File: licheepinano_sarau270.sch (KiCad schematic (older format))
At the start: 0 parts

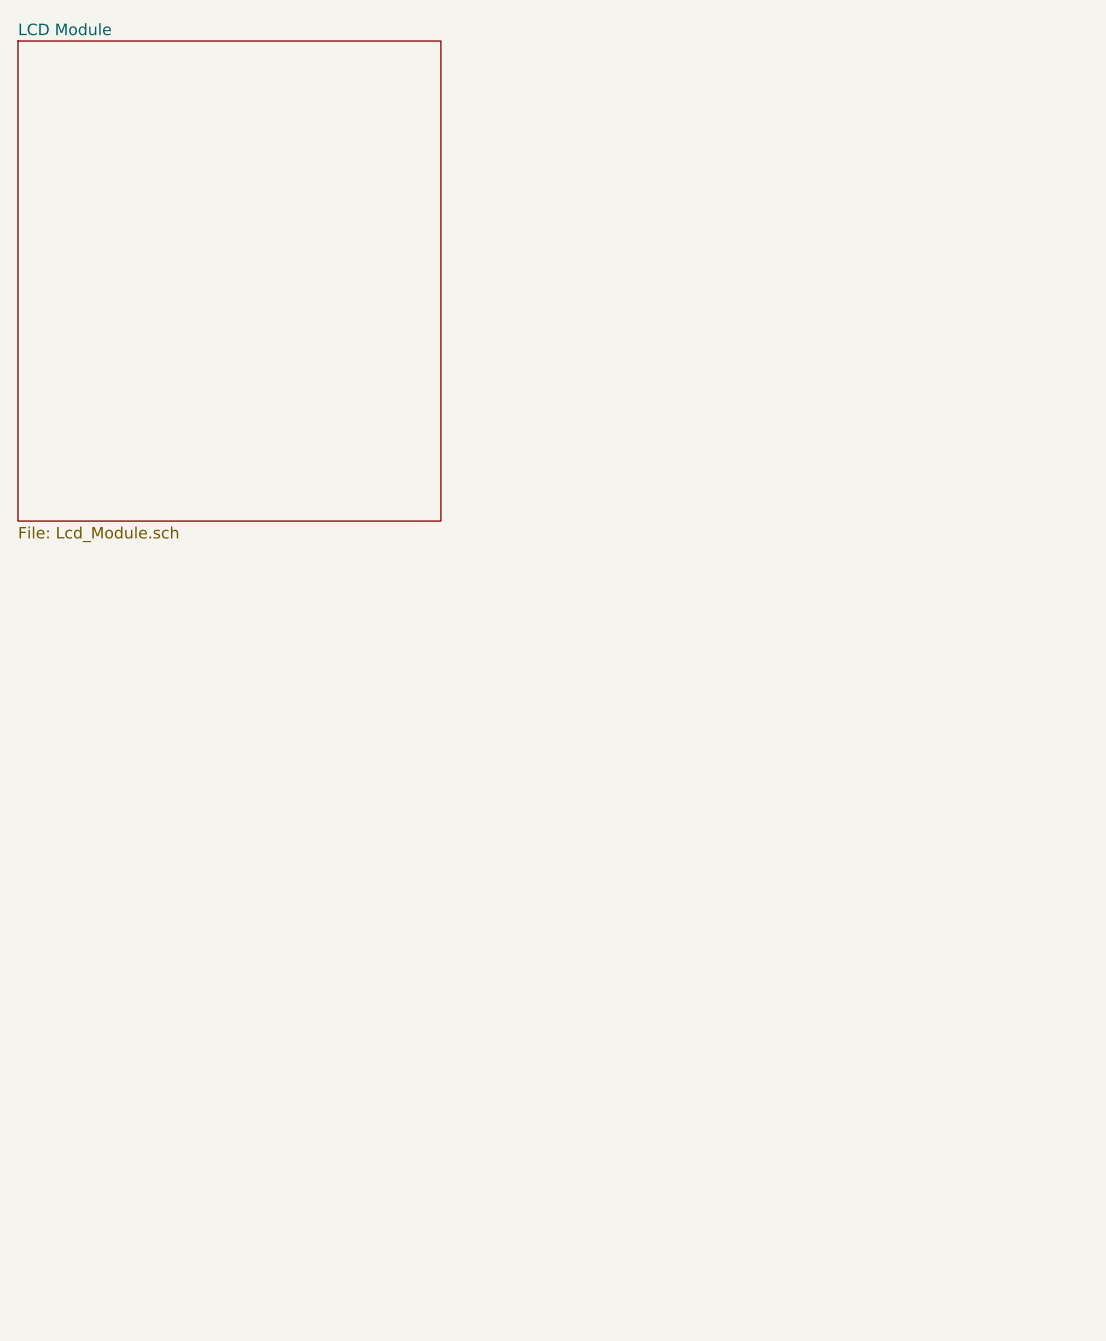
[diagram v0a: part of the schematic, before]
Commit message: Added Hub USB, Modem 3G and GPS
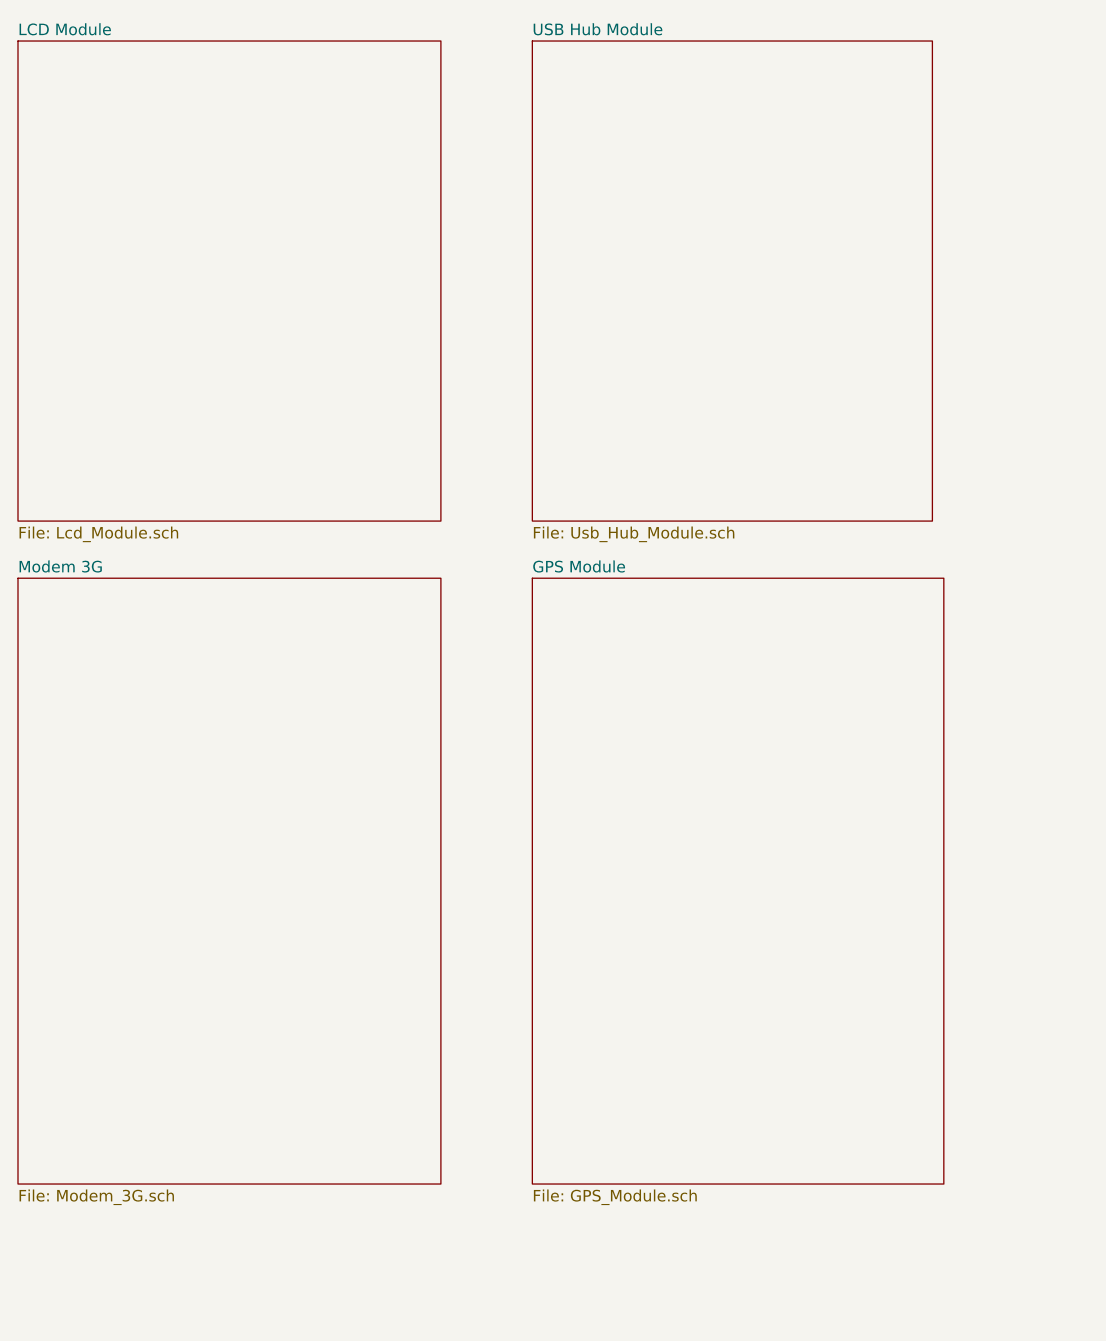
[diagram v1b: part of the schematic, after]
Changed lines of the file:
@@
 $Descr A3 16535 11693
 encoding utf-8
-Sheet 1 3
+Sheet 1 6
 Title "LicheePi Nano Sara U270 Development Board"
 Date "2020-11-14"
@@
 F1 "Lcd_Module.sch" 50
 $EndSheet
+$Sheet
+S 5250 1900 1750 2100
+U 5FB1924B
+F0 "USB Hub Module" 50
+F1 "Usb_Hub_Module.sch" 50
+$EndSheet
+$Sheet
+S 3000 4250 1850 2650
+U 5FB33D69
+F0 "Modem 3G" 50
+F1 "Modem_3G.sch" 50
+$EndSheet
+$Sheet
+S 5250 4250 1800 2650
+U 5FB342F4
+F0 "GPS Module" 50
+F1 "GPS_Module.sch" 50
+$EndSheet
 $EndSCHEMATC

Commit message: Updated schematic
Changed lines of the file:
@@
 F0 "GPS Module" 50
 F1 "GPS_Module.sch" 50
+F2 "~GPS_RESET" I R 7050 4450 50
+F3 "GNSS_ENABLE" I R 7050 4600 50
+F4 "I2C_1V8_SCL" I R 7050 4750 50
+F5 "I2C_1V8_SDA" B R 7050 4900 50
+F6 "UART_GPS_1V8_RXD" I R 7050 5050 50
+F7 "UART_GPS_1V8_TXD" O R 7050 5200 50
+F8 "GPS_EXTINT" I R 7050 5350 50
+F9 "GPS_V_BCKP" I R 7050 5500 50
+F10 "POWER_IN_1V8" I R 7050 5600 50
+F11 "POWER_IN_GND" I R 7050 5700 50
 $EndSheet
 $EndSCHEMATC

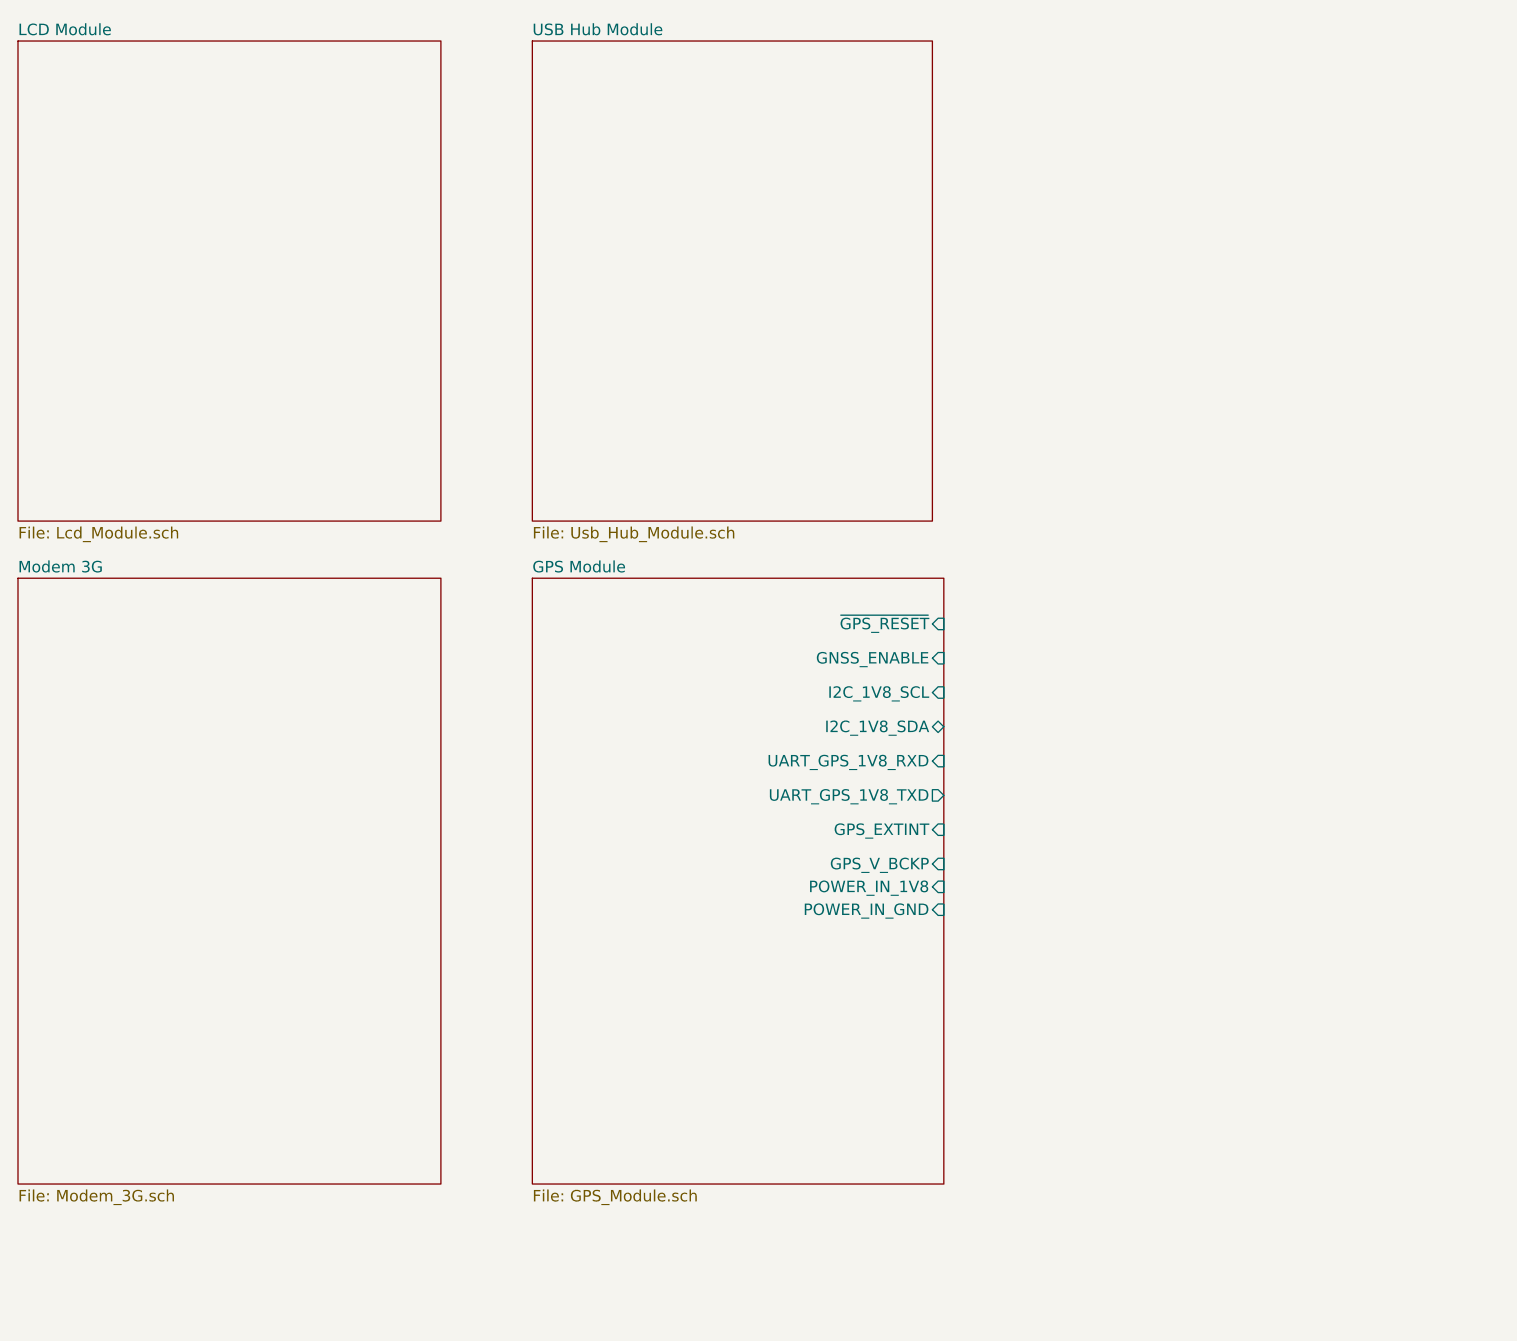
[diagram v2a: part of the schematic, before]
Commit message: Added logic level shifter on pcb
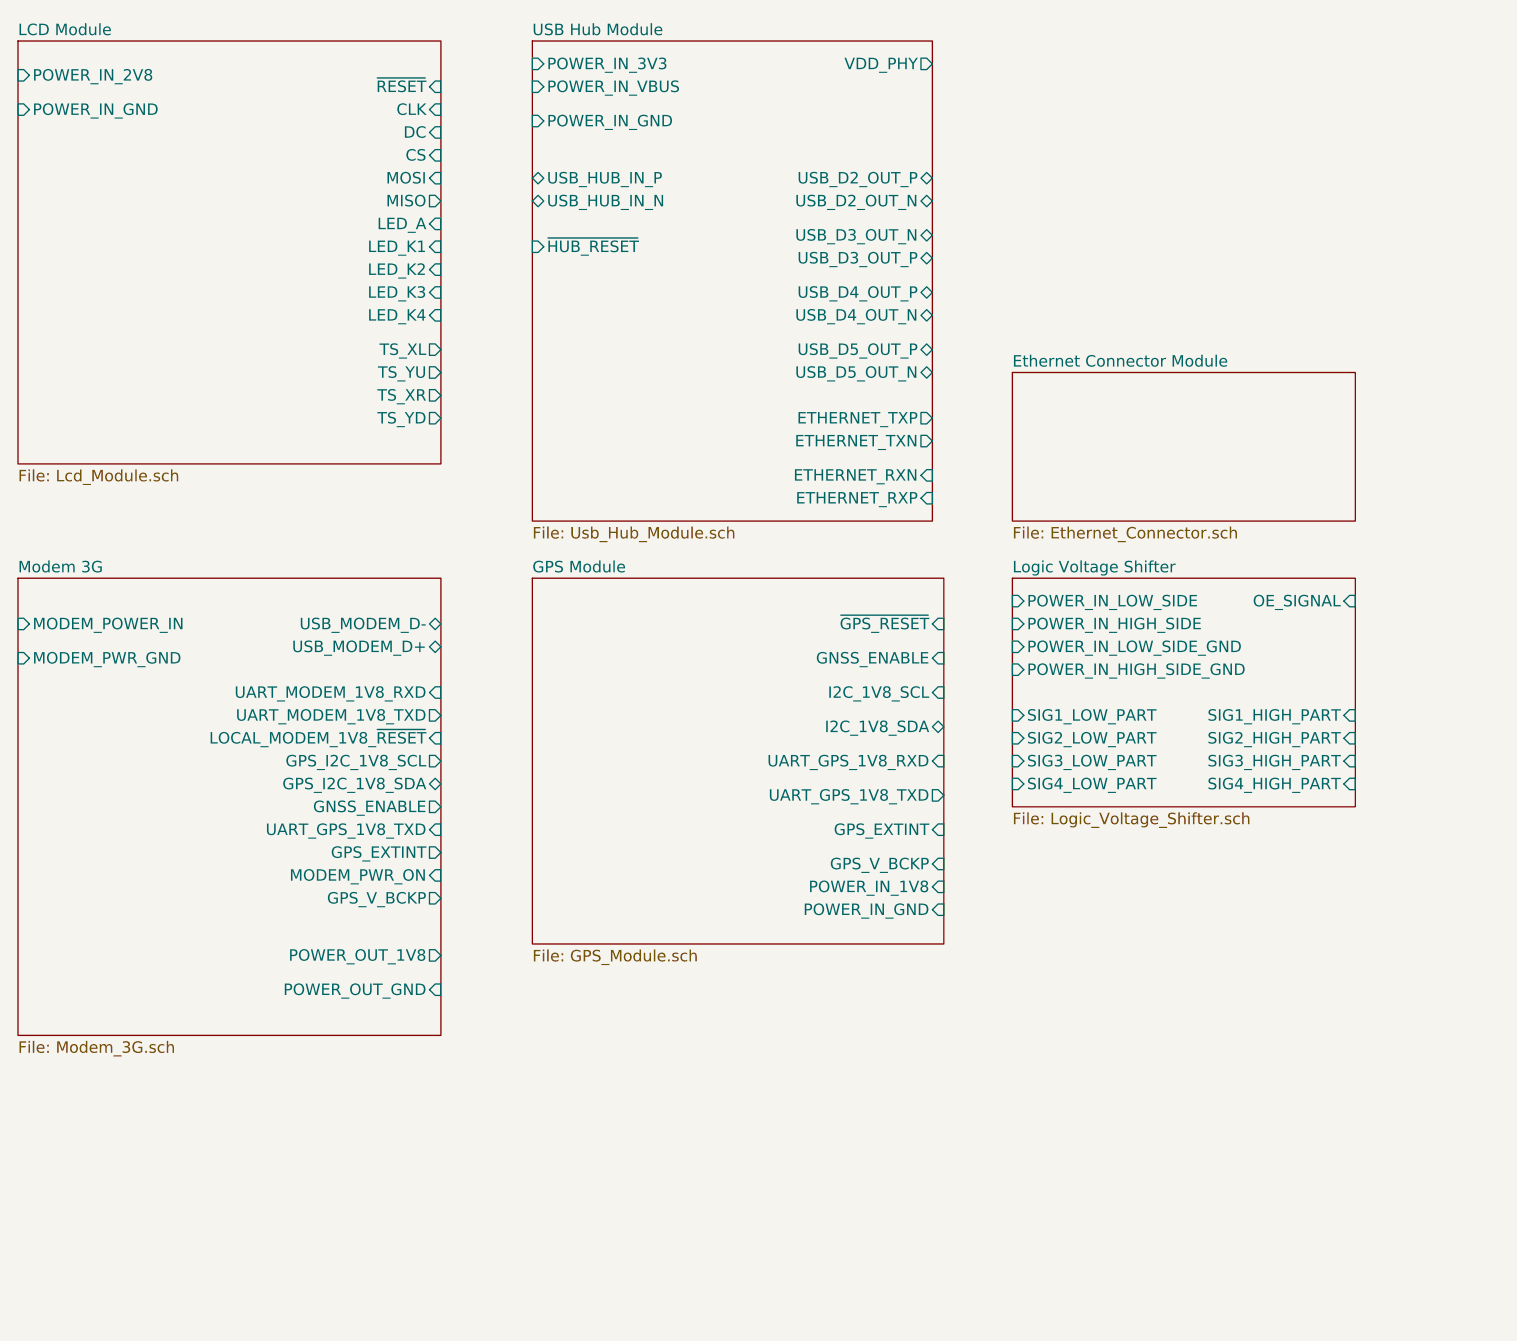
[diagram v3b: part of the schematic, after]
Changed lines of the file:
@@
 $Descr A3 16535 11693
 encoding utf-8
-Sheet 1 6
+Sheet 1 8
 Title "LicheePi Nano Sara U270 Development Board"
 Date "2020-11-14"
@@
 $EndSheet
 $Sheet
-S 3000 1900 1850 2100
+S 3000 1900 1850 1850
 U 5FB02458
 F0 "LCD Module" 50
 F1 "Lcd_Module.sch" 50
+F2 "POWER_IN_2V8" I L 3000 2050 50
+F3 "POWER_IN_GND" I L 3000 2200 50
+F4 "~RESET" I R 4850 2100 50
+F5 "CLK" I R 4850 2200 50
+F6 "DC" I R 4850 2300 50
+F7 "CS" I R 4850 2400 50
+F8 "MOSI" I R 4850 2500 50
+F9 "MISO" O R 4850 2600 50
+F10 "LED_A" I R 4850 2700 50
+F11 "LED_K1" I R 4850 2800 50
+F12 "LED_K2" I R 4850 2900 50
+F13 "LED_K3" I R 4850 3000 50
+F14 "LED_K4" I R 4850 3100 50
+F15 "TS_XL" O R 4850 3250 50
+F16 "TS_YU" O R 4850 3350 50
+F17 "TS_XR" O R 4850 3450 50
+F18 "TS_YD" O R 4850 3550 50
 $EndSheet
 $Sheet
@@
 F0 "USB Hub Module" 50
 F1 "Usb_Hub_Module.sch" 50
+F2 "USB_HUB_IN_P" B L 5250 2500 50
+F3 "USB_HUB_IN_N" B L 5250 2600 50
+F4 "USB_D5_OUT_N" B R 7000 3350 50
+F5 "USB_D5_OUT_P" B R 7000 3250 50
+F6 "USB_D3_OUT_P" B R 7000 2850 50
+F7 "USB_D3_OUT_N" B R 7000 2750 50
+F8 "USB_D4_OUT_P" B R 7000 3000 50
+F9 "USB_D4_OUT_N" B R 7000 3100 50
+F10 "USB_D2_OUT_P" B R 7000 2500 50
+F11 "USB_D2_OUT_N" B R 7000 2600 50
+F12 "~HUB_RESET" I L 5250 2800 50
+F13 "ETHERNET_TXP" O R 7000 3550 50
+F14 "ETHERNET_TXN" O R 7000 3650 50
+F15 "ETHERNET_RXN" I R 7000 3800 50
+F16 "ETHERNET_RXP" I R 7000 3900 50
+F17 "VDD_PHY" O R 7000 2000 50
+F18 "POWER_IN_3V3" I L 5250 2000 50
+F19 "POWER_IN_VBUS" I L 5250 2100 50
+F20 "POWER_IN_GND" I L 5250 2250 50
 $EndSheet
 $Sheet
-S 3000 4250 1850 2650
+S 3000 4250 1850 2000
 U 5FB33D69
 F0 "Modem 3G" 50
 F1 "Modem_3G.sch" 50
+F2 "USB_MODEM_D-" B R 4850 4450 50
+F3 "USB_MODEM_D+" B R 4850 4550 50
+F4 "UART_MODEM_1V8_RXD" I R 4850 4750 50
+F5 "UART_MODEM_1V8_TXD" O R 4850 4850 50
+F6 "LOCAL_MODEM_1V8_~RESET" I R 4850 4950 50
+F7 "GPS_I2C_1V8_SCL" O R 4850 5050 50
+F8 "GPS_I2C_1V8_SDA" B R 4850 5150 50
+F9 "GNSS_ENABLE" O R 4850 5250 50
+F10 "UART_GPS_1V8_TXD" I R 4850 5350 50
+F11 "GPS_EXTINT" O R 4850 5450 50
+F12 "MODEM_PWR_ON" I R 4850 5550 50
+F13 "GPS_V_BCKP" O R 4850 5650 50
+F14 "MODEM_POWER_IN" I L 3000 4450 50
+F15 "MODEM_PWR_GND" I L 3000 4600 50
+F16 "POWER_OUT_1V8" O R 4850 5900 50
+F17 "POWER_OUT_GND" I R 4850 6050 50
 $EndSheet
 $Sheet
-S 5250 4250 1800 2650
+S 5250 4250 1800 1600
 U 5FB342F4
 F0 "GPS Module" 50
@@
 F11 "POWER_IN_GND" I R 7050 5700 50
 $EndSheet
+$Sheet
+S 7350 4250 1500 1000
+U 5FC54F14
+F0 "Logic Voltage Shifter" 50
+F1 "Logic_Voltage_Shifter.sch" 50
+F2 "POWER_IN_LOW_SIDE" I L 7350 4350 50
+F3 "POWER_IN_HIGH_SIDE" I L 7350 4450 50
+F4 "POWER_IN_LOW_SIDE_GND" I L 7350 4550 50
+F5 "POWER_IN_HIGH_SIDE_GND" I L 7350 4650 50
+F6 "OE_SIGNAL" I R 8850 4350 50
+F7 "SIG1_LOW_PART" I L 7350 4850 50
+F8 "SIG2_LOW_PART" I L 7350 4950 50
+F9 "SIG3_LOW_PART" I L 7350 5050 50
+F10 "SIG4_LOW_PART" I L 7350 5150 50
+F11 "SIG4_HIGH_PART" I R 8850 5150 50
+F12 "SIG3_HIGH_PART" I R 8850 5050 50
+F13 "SIG2_HIGH_PART" I R 8850 4950 50
+F14 "SIG1_HIGH_PART" I R 8850 4850 50
+$EndSheet
+$Sheet
+S 7350 3350 1500 650
+U 5FBCC428
+F0 "Ethernet Connector Module" 50
+F1 "Ethernet_Connector.sch" 50
+$EndSheet
 $EndSCHEMATC
